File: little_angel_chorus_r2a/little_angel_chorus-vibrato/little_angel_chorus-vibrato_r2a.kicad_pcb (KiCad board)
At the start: 2 copper layers, 58.4 x 81.3 mm, 118 parts, among them J1 X, J10 X, J2 0, J3 X, J4 X, J5 0, J6 0, J7 0, J8 0, J9 0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

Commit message: Little Angel Chorus [REV2A]: remaining output files added
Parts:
- IB.J1: value 0 -> X
- IB.J2, IB.J3: value X -> 0
- IB.R2: value 474 -> 223
- IB.R3: value 334 -> 474
- IB.R4: value 105 -> 223

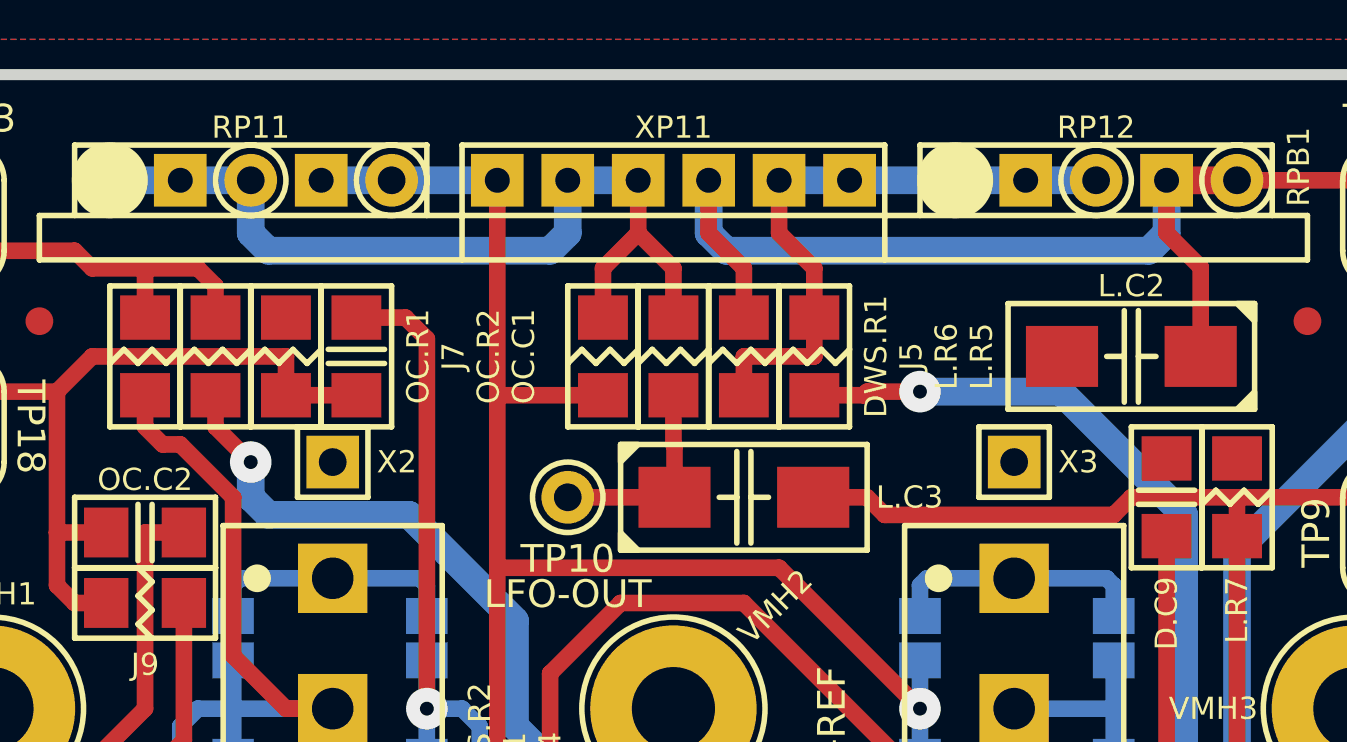
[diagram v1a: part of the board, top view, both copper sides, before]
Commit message: Little Angel Chorus [REV2A]: purposes and values of DWS.R1 and L.R6 changed
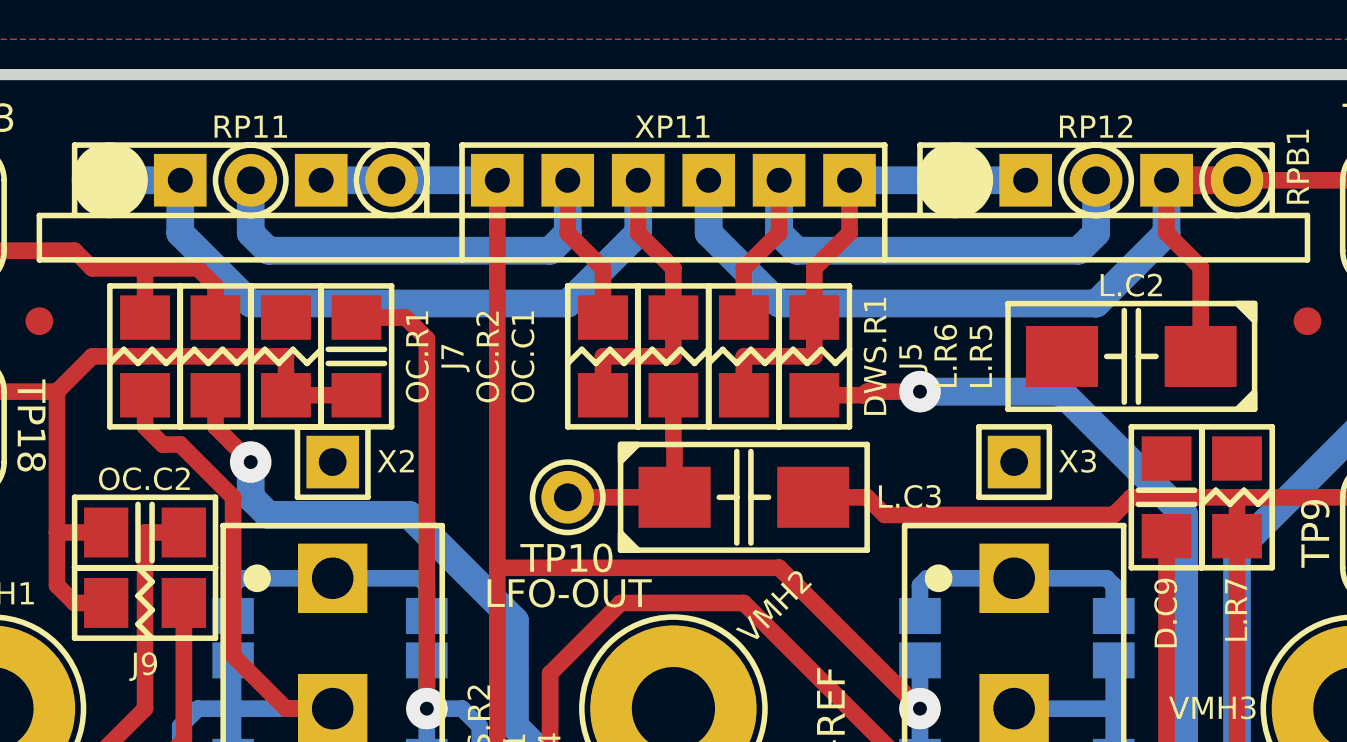
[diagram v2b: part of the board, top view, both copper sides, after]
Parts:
- DWS.R1, L.R6: value X -> 0
- turned DWS.R1 to 90 degrees
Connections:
- DWS.R1 pad 2: Net-(DWS.J3-Pad2) -> Net-(DWS.R1-Pad2)
- L.R6 pad 2: /LFO-B-IN -> Net-(L.R6-Pad2)
- RPB1 pad 12: /DEPTH-IN -> Net-(DWS.R1-Pad2)
- RPB1 pad 22: Net-(L.R5-Pad2) -> Net-(L.R6-Pad2)
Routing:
- net Net-(L.R6-Pad2): track 0.00 -> 21.2 mm
- net Net-(DWS.R1-Pad2): track 0.00 -> 21.2 mm
- net Net-(L.R5-Pad2): track 22.2 -> 17.2 mm
- net /LFO-B-IN: track 84.6 -> 80.7 mm
- net Net-(DWS.J3-Pad2): track 55.0 -> 51.2 mm
- net /DEPTH-IN: track 32.4 -> 35.8 mm

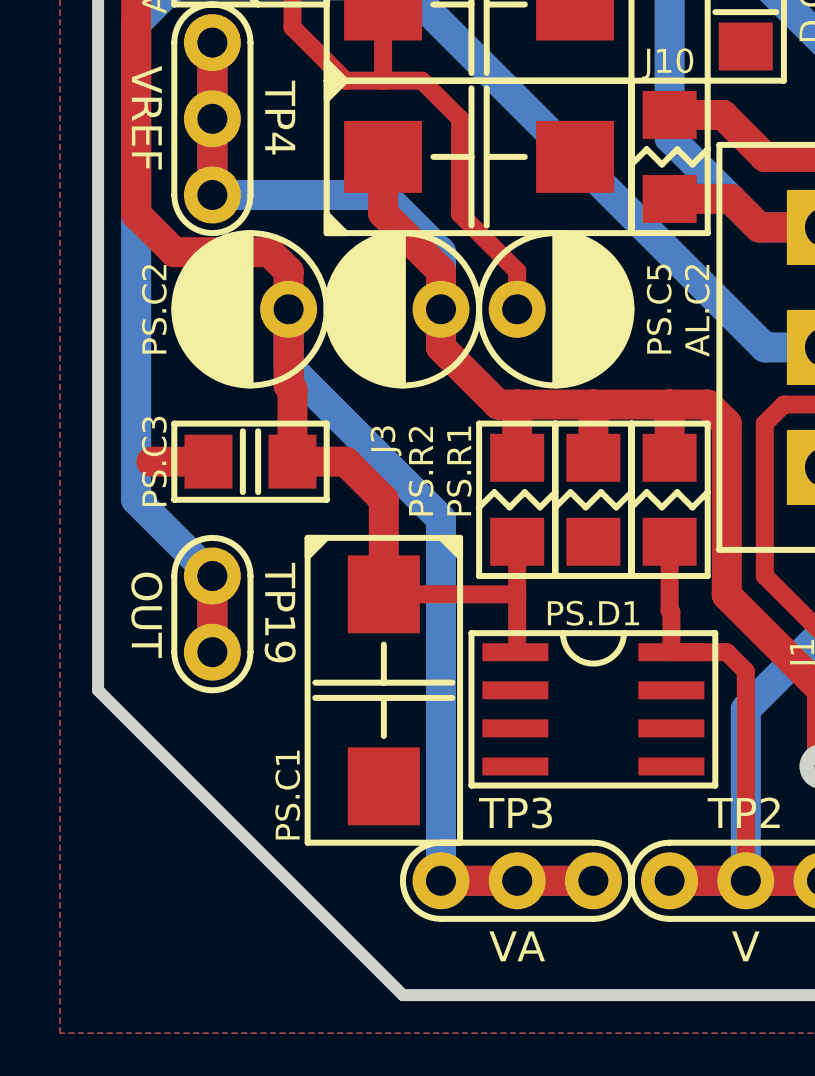
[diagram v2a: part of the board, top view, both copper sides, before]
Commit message: Little Angel Chorus [REV2A]: PS.C5 rotated
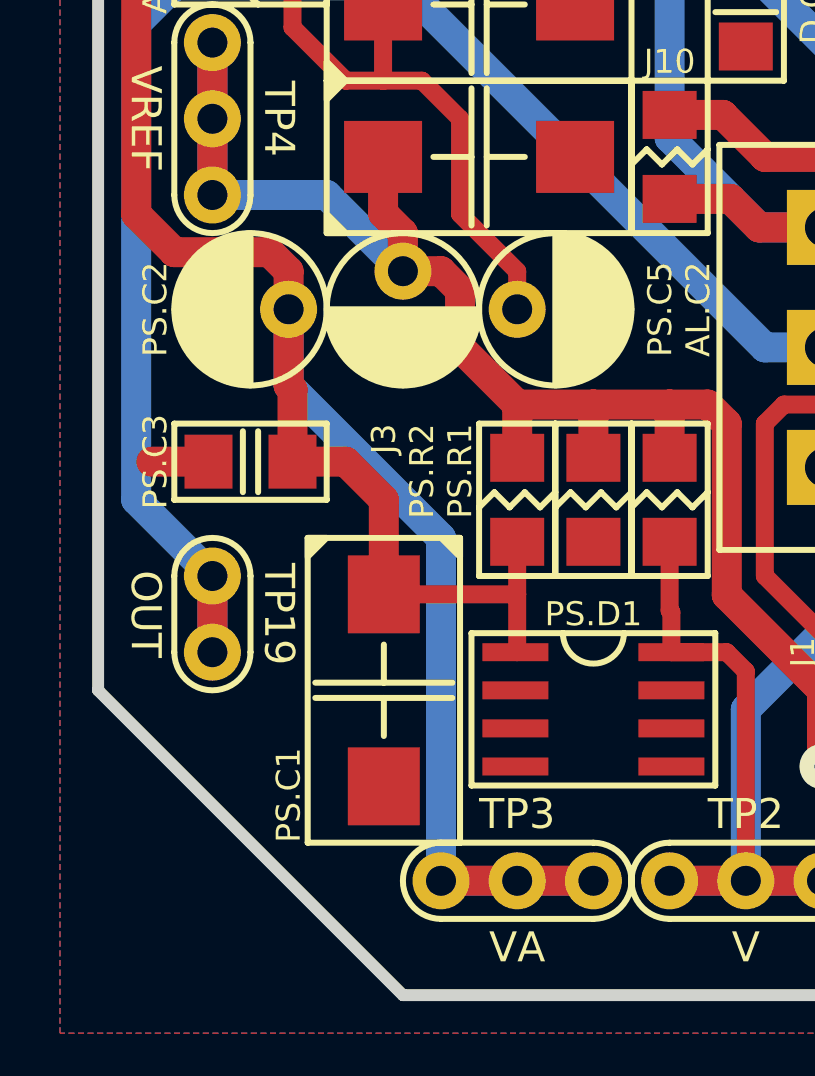
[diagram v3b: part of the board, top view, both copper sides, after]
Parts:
- turned PS.C5 to 270 degrees
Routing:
- net VREF: track 82.3 -> 79.8 mm

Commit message: Minor changes
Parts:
- VFM1, VFM2, VFM3: footprint KCL-VIRTUAL:VFM-1.0-3.0 -> KCL-VIRTUAL:VFM-1.0-3.0-SL
